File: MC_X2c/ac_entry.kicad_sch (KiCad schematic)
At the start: 16 parts, among them U1 R-78E3.3-1.0

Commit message: Working progress - migration to MAC
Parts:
- renumbered U1 to U2
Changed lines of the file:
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@@
 	(title_block
 		(title "AC Entry")
-		(date "2025-06-1")
+		(date "2025-06-27")
 		(rev "1.0")
 		(company "Nelees")
@@
 		(dnp no)
 		(fields_autoplaced yes)
-		(property "Reference" "U1"
+		(property "Reference" "U2"
 			(at 194.31 36.83 0)
 			(effects
@@
 			(project "MC_X2c"
 				(path "/7c61db7a-af98-4251-97f0-4a36956e03cd/b18795d0-8482-4f6f-8249-1321515800c6"
-					(reference "U1")
-					(unit 1)
-				)
+					(reference "U2")
+					(unit 1)
+				)

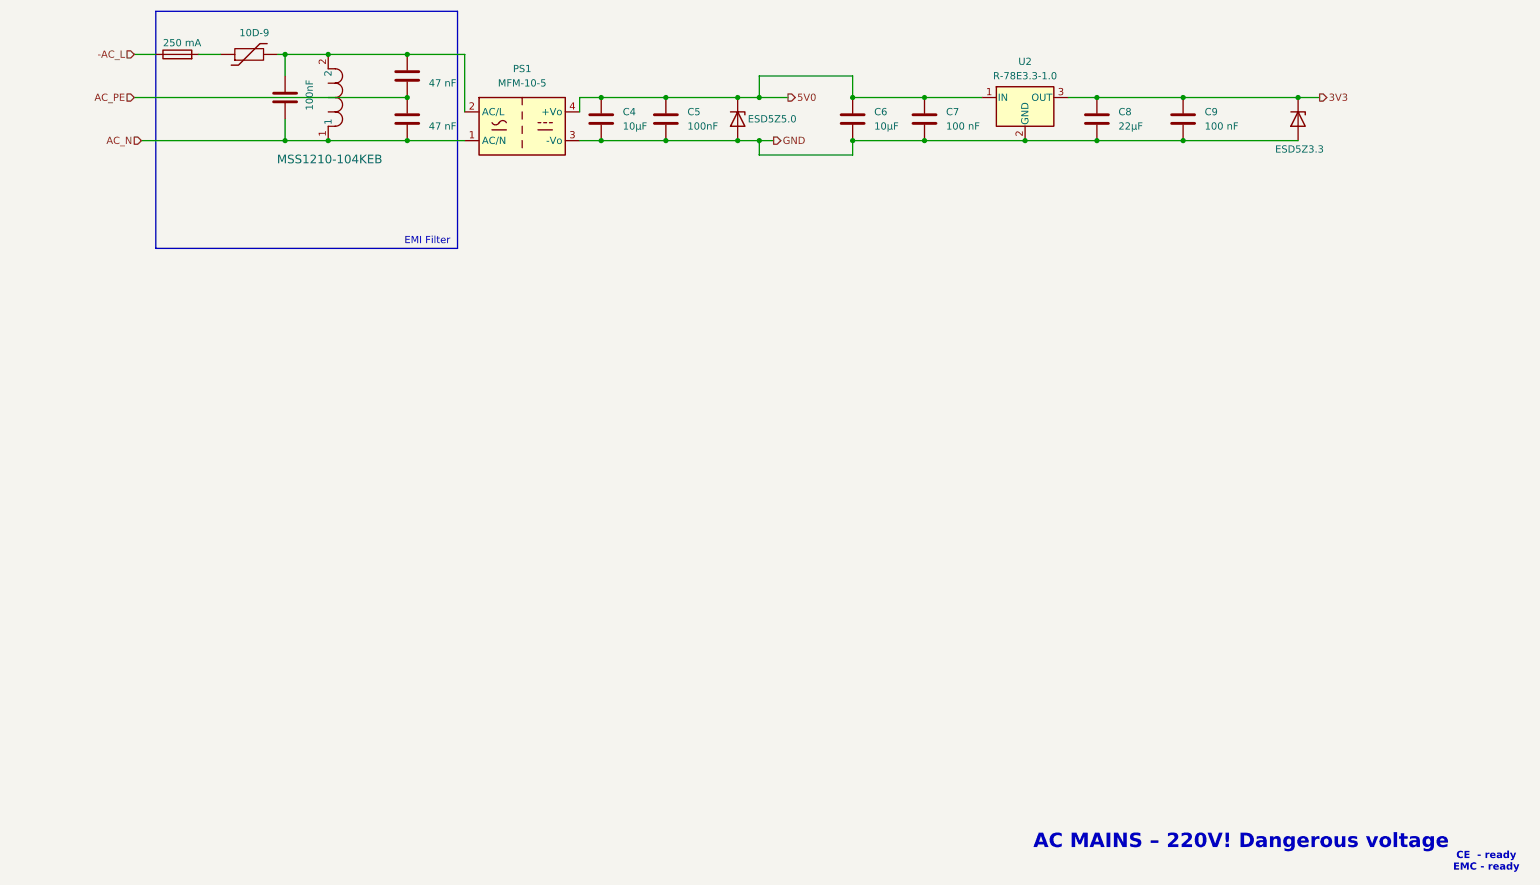
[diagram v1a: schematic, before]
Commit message: Proper namings in AC_ENTRY and CHANNEL + passives on root
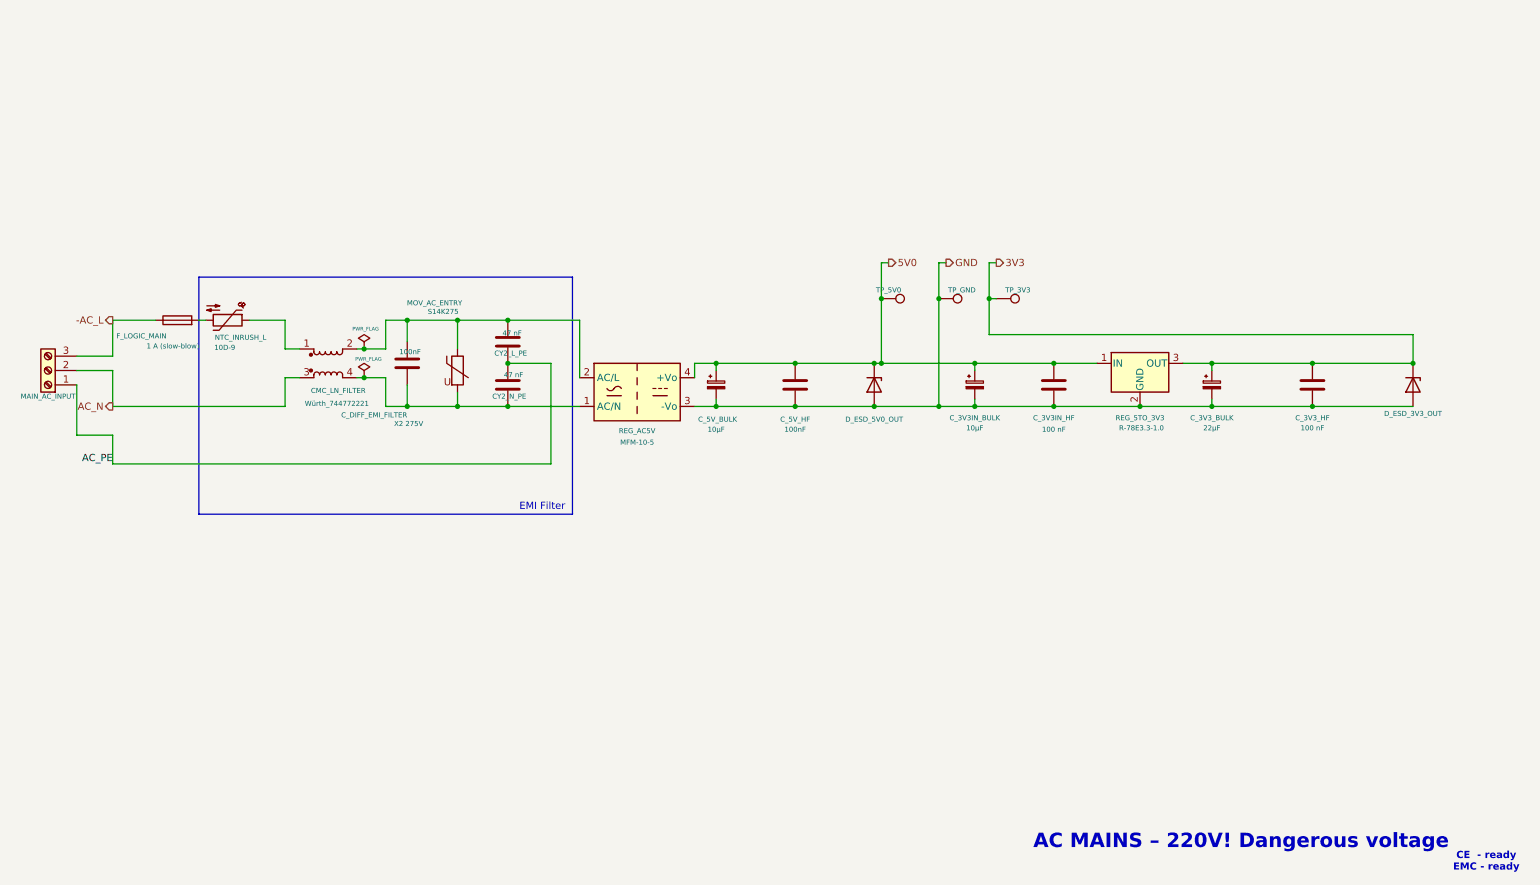
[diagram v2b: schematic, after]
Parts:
- removed C6: 10µF, symbol Device:C
- removed L1: MSS1210-104KEB, IND_MSS1210_COC, symbol nelees:MSS1210-104KEB
- removed TH1: 10D-9, symbol Device:Thermistor
- added CMC_LN_FILTER: Würth_744772221, Inductor_SMD:L_Wuerth_WE-DD-Typ-L-Typ-XL-Typ-XXL, symbol Device:L_Coupled
- added C_3V3IN_BULK: 10µF, symbol Device:C_Polarized_Small
- added MAIN_AC_INPUT: Screw_Terminal_01x03, symbol Connector:Screw_Terminal_01x03
- added MOV_AC_ENTRY: S14K275, symbol Device:Varistor
- added NTC_INRUSH_L: 10D-9, symbol Device:Thermistor_NTC
- added TP2: TP_3V3, TestPoint:TestPoint_Pad_1.0x1.0mm, symbol Connector:TestPoint
- added TP3: TP_GND, TestPoint:TestPoint_Pad_1.0x1.0mm, symbol Connector:TestPoint
- added TP_5V0: TP_5V0, TestPoint:TestPoint_Pad_1.0x1.0mm, symbol Connector:TestPoint
- C_3V3_BULK: renamed from C8; symbol Device:C -> Device:C_Polarized_Small
- C_5V_BULK: renamed from C4; symbol Device:C -> Device:C_Polarized_Small
- D_ESD_5V0_OUT: renamed from D1; value ESD5Z5.0 -> D_ESD_5V0_OUT
- F_LOGIC_MAIN: renamed from F1; value 250 mA -> 1 A (slow-blow)
- renumbered C2 to CY2_L_PE, C3 to CY2_N_PE, C7 to C_3V3IN_HF, C9 to C_3V3_HF, C5 to C_5V_HF, C1 to C_DIFF_EMI_FILTER, D2 to D_ESD_3V3_OUT, U2 to REG_5TO_3V3, PS1 to REG_AC5V
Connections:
- net 3V3: now also TP2.1
- net 5V0: now also C_3V3IN_BULK.1, TP_5V0.1
- net AC_N: now also CMC_LN_FILTER.3, MAIN_AC_INPUT.2 (Pin_2); no longer CY2_N_PE.2, C_DIFF_EMI_FILTER.2, REG_AC5V.1 (AC/N)
- net AC_PE: now also MAIN_AC_INPUT.1 (Pin_1)
- net GND: now also C_3V3IN_BULK.2, TP3.1
- net ­AC_L: now also MAIN_AC_INPUT.3 (Pin_3)
- net at F_LOGIC_MAIN.2: now also NTC_INRUSH_L.2
- net at CY2_L_PE.1, C_DIFF_EMI_FILTER.1, REG_AC5V.2 (AC/L): now also CMC_LN_FILTER.2, MOV_AC_ENTRY.1
- new net: CMC_LN_FILTER.1, NTC_INRUSH_L.1
- new net: CMC_LN_FILTER.4, CY2_N_PE.2, C_DIFF_EMI_FILTER.2, MOV_AC_ENTRY.2, REG_AC5V.1 (AC/N)
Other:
- moved on the sheet: C_3V3IN_HF, C_3V3_HF, C_5V_HF, REG_5TO_3V3, REG_AC5V

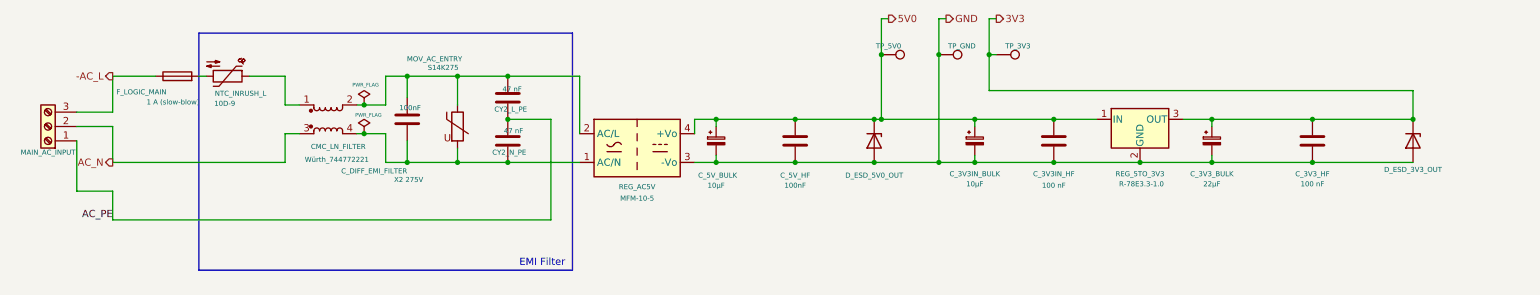
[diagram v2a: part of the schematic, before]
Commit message: Fix channel refference names and add fuse for channel out
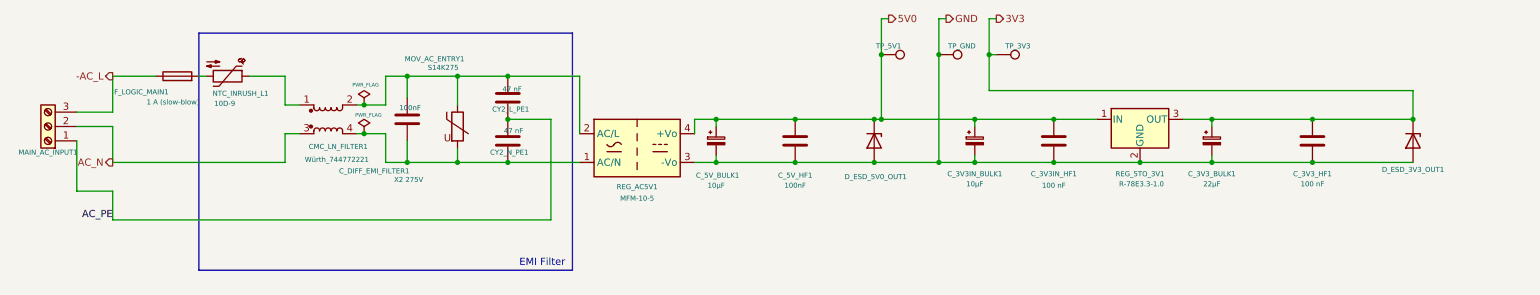
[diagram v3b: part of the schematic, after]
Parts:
- renumbered CMC_LN_FILTER to CMC_LN_FILTER1, CY2_L_PE to CY2_L_PE1, CY2_N_PE to CY2_N_PE1, C_3V3IN_BULK to C_3V3IN_BULK1, C_3V3IN_HF to C_3V3IN_HF1, C_3V3_BULK to C_3V3_BULK1, C_3V3_HF to C_3V3_HF1, C_5V_BULK to C_5V_BULK1, C_5V_HF to C_5V_HF1, C_DIFF_EMI_FILTER to C_DIFF_EMI_FILTER1, D_ESD_3V3_OUT to D_ESD_3V3_OUT1, D_ESD_5V0_OUT to D_ESD_5V0_OUT1, F_LOGIC_MAIN to F_LOGIC_MAIN1, MAIN_AC_INPUT to MAIN_AC_INPUT1, MOV_AC_ENTRY to MOV_AC_ENTRY1, NTC_INRUSH_L to NTC_INRUSH_L1, REG_5TO_3V3 to REG_5TO_3V1, REG_AC5V to REG_AC5V1, TP3 to TP1, TP_5V0 to TP_5V1
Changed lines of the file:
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@@
 		(on_board yes)
 		(dnp no)
-		(property "Reference" "F_LOGIC_MAIN"
+		(property "Reference" "F_LOGIC_MAIN1"
 			(at 38.1 85.344 90)
 			(effects
@@
 			(project "MC_X2c"
 				(path "/7c61db7a-af98-4251-97f0-4a36956e03cd/b18795d0-8482-4f6f-8249-1321515800c6"
-					(reference "F_LOGIC_MAIN")
+					(reference "F_LOGIC_MAIN1")
 					(unit 1)
 				)
@@
 		(on_board yes)
 		(dnp no)
-		(property "Reference" "D_ESD_5V0_OUT"
-			(at 173.99 93.98 0)
-			(effects
-				(font
-					(size 0.889 0.889)
-				)
-				(hide yes)
+		(property "Reference" "D_ESD_5V0_OUT1"
+			(at 167.894 100.33 90)
+			(effects
+				(font
+					(size 0.889 0.889)
+				)
 			)
 		)
 		(property "Value" "D_ESD_5V0_OUT"
-			(at 167.64 100.076 90)
-			(effects
-				(font
-					(size 0.889 0.889)
-					(color 179 61 255 1)
-				)
+			(at 168.148 102.616 90)
+			(effects
+				(font
+					(size 0.889 0.889)
+					(color 179 61 255 1)
+				)
+				(hide yes)
 			)
 		)
@@
 			(project "MC_X2c"
 				(path "/7c61db7a-af98-4251-97f0-4a36956e03cd/b18795d0-8482-4f6f-8249-1321515800c6"
-					(reference "D_ESD_5V0_OUT")
+					(reference "D_ESD_5V0_OUT1")
 					(unit 1)
 				)
@@
 		(on_board yes)
 		(dnp no)
-		(property "Reference" "CMC_LN_FILTER"
+		(property "Reference" "CMC_LN_FILTER1"
 			(at 72.898 94.996 0)
 			(effects
@@
 			(project ""
 				(path "/7c61db7a-af98-4251-97f0-4a36956e03cd/b18795d0-8482-4f6f-8249-1321515800c6"
-					(reference "CMC_LN_FILTER")
+					(reference "CMC_LN_FILTER1")
 					(unit 1)
 				)
@@
 		(on_board yes)
 		(dnp no)
-		(property "Reference" "REG_AC5V"
+		(property "Reference" "REG_AC5V1"
 			(at 125.73 102.108 0)
 			(effects
@@
 			(project "MC_X2c"
 				(path "/7c61db7a-af98-4251-97f0-4a36956e03cd/b18795d0-8482-4f6f-8249-1321515800c6"
-					(reference "REG_AC5V")
+					(reference "REG_AC5V1")
 					(unit 1)
 				)
@@
 		(on_board yes)
 		(dnp no)
-		(property "Reference" "C_3V3IN_HF"
+		(property "Reference" "C_3V3IN_HF1"
 			(at 199.39 99.822 0)
 			(effects
@@
 			(project "MC_X2c"
 				(path "/7c61db7a-af98-4251-97f0-4a36956e03cd/b18795d0-8482-4f6f-8249-1321515800c6"
-					(reference "C_3V3IN_HF")
+					(reference "C_3V3IN_HF1")
 					(unit 1)
 				)
@@
 		(on_board yes)
 		(dnp no)
-		(property "Reference" "CY2_L_PE"
+		(property "Reference" "CY2_L_PE1"
 			(at 103.378 88.392 0)
 			(effects
@@
 			(project "MC_X2c"
 				(path "/7c61db7a-af98-4251-97f0-4a36956e03cd/b18795d0-8482-4f6f-8249-1321515800c6"
-					(reference "CY2_L_PE")
+					(reference "CY2_L_PE1")
 					(unit 1)
 				)
@@
 		(on_board yes)
 		(dnp no)
-		(property "Reference" "NTC_INRUSH_L"
+		(property "Reference" "NTC_INRUSH_L1"
 			(at 55.626 85.598 90)
 			(effects
@@
 			(project ""
 				(path "/7c61db7a-af98-4251-97f0-4a36956e03cd/b18795d0-8482-4f6f-8249-1321515800c6"
-					(reference "NTC_INRUSH_L")
+					(reference "NTC_INRUSH_L1")
 					(unit 1)
 				)
@@
 		(on_board yes)
 		(dnp no)
-		(property "Reference" "REG_5TO_3V3"
+		(property "Reference" "REG_5TO_3V1"
 			(at 214.63 99.822 0)
 			(effects
@@
 			(project "MC_X2c"
 				(path "/7c61db7a-af98-4251-97f0-4a36956e03cd/b18795d0-8482-4f6f-8249-1321515800c6"
-					(reference "REG_5TO_3V3")
+					(reference "REG_5TO_3V1")
 					(unit 1)
 				)
@@
 		(on_board yes)
 		(dnp no)
-		(property "Reference" "TP_5V0"
+		(property "Reference" "TP_5V1"
 			(at 170.18 77.216 90)
 			(effects
@@
 			(project ""
 				(path "/7c61db7a-af98-4251-97f0-4a36956e03cd/b18795d0-8482-4f6f-8249-1321515800c6"
-					(reference "TP_5V0")
+					(reference "TP_5V1")
 					(unit 1)
 				)
@@
 		(on_board yes)
 		(dnp no)
-		(property "Reference" "CY2_N_PE"
+		(property "Reference" "CY2_N_PE1"
 			(at 103.124 96.012 0)
 			(effects
@@
 			(project "MC_X2c"
 				(path "/7c61db7a-af98-4251-97f0-4a36956e03cd/b18795d0-8482-4f6f-8249-1321515800c6"
-					(reference "CY2_N_PE")
+					(reference "CY2_N_PE1")
 					(unit 1)
 				)
@@
 		(on_board yes)
 		(dnp no)
-		(property "Reference" "C_3V3IN_BULK"
+		(property "Reference" "C_3V3IN_BULK1"
 			(at 185.42 99.822 0)
 			(effects
@@
 			(project "MC_X2c"
 				(path "/7c61db7a-af98-4251-97f0-4a36956e03cd/b18795d0-8482-4f6f-8249-1321515800c6"
-					(reference "C_3V3IN_BULK")
+					(reference "C_3V3IN_BULK1")
 					(unit 1)
 				)
@@
 		(on_board yes)
 		(dnp no)
-		(property "Reference" "TP3"
+		(property "Reference" "TP1"
 			(at 183.6421 81.28 0)
 			(effects
@@
 			(project "MC_X2c"
 				(path "/7c61db7a-af98-4251-97f0-4a36956e03cd/b18795d0-8482-4f6f-8249-1321515800c6"
-					(reference "TP3")
+					(reference "TP1")
 					(unit 1)
 				)
@@
 		(on_board yes)
 		(dnp no)
-		(property "Reference" "C_DIFF_EMI_FILTER"
+		(property "Reference" "C_DIFF_EMI_FILTER1"
 			(at 79.248 99.314 0)
 			(effects
@@
 			(project "MC_X2c"
 				(path "/7c61db7a-af98-4251-97f0-4a36956e03cd/b18795d0-8482-4f6f-8249-1321515800c6"
-					(reference "C_DIFF_EMI_FILTER")
+					(reference "C_DIFF_EMI_FILTER1")
 					(unit 1)
 				)
@@
 		(on_board yes)
 		(dnp no)
-		(property "Reference" "MAIN_AC_INPUT"
+		(property "Reference" "MAIN_AC_INPUT1"
 			(at 21.59 96.012 0)
 			(effects
@@
 			(project ""
 				(path "/7c61db7a-af98-4251-97f0-4a36956e03cd/b18795d0-8482-4f6f-8249-1321515800c6"
-					(reference "MAIN_AC_INPUT")
+					(reference "MAIN_AC_INPUT1")
 					(unit 1)
 				)
@@
 		(on_board yes)
 		(dnp no)
-		(property "Reference" "D_ESD_3V3_OUT"
+		(property "Reference" "D_ESD_3V3_OUT1"
 			(at 262.89 99.06 90)
 			(effects
@@
 			(project "MC_X2c"
 				(path "/7c61db7a-af98-4251-97f0-4a36956e03cd/b18795d0-8482-4f6f-8249-1321515800c6"
-					(reference "D_ESD_3V3_OUT")
+					(reference "D_ESD_3V3_OUT1")
 					(unit 1)
 				)
@@
 		(on_board yes)
 		(dnp no)
-		(property "Reference" "C_5V_BULK"
+		(property "Reference" "C_5V_BULK1"
 			(at 139.954 100.076 0)
 			(effects
@@
 			(project "MC_X2c"
 				(path "/7c61db7a-af98-4251-97f0-4a36956e03cd/b18795d0-8482-4f6f-8249-1321515800c6"
-					(reference "C_5V_BULK")
+					(reference "C_5V_BULK1")
 					(unit 1)
 				)
@@
 		(on_board yes)
 		(dnp no)
-		(property "Reference" "C_5V_HF"
+		(property "Reference" "C_5V_HF1"
 			(at 153.67 100.076 0)
 			(effects
@@
 			(project "MC_X2c"
 				(path "/7c61db7a-af98-4251-97f0-4a36956e03cd/b18795d0-8482-4f6f-8249-1321515800c6"
-					(reference "C_5V_HF")
+					(reference "C_5V_HF1")
 					(unit 1)
 				)
@@
 		(on_board yes)
 		(dnp no)
-		(property "Reference" "MOV_AC_ENTRY"
+		(property "Reference" "MOV_AC_ENTRY1"
 			(at 89.916 79.502 0)
 			(effects
@@
 			(project ""
 				(path "/7c61db7a-af98-4251-97f0-4a36956e03cd/b18795d0-8482-4f6f-8249-1321515800c6"
-					(reference "MOV_AC_ENTRY")
+					(reference "MOV_AC_ENTRY1")
 					(unit 1)
 				)
@@
 		(on_board yes)
 		(dnp no)
-		(property "Reference" "C_3V3_HF"
+		(property "Reference" "C_3V3_HF1"
 			(at 245.11 99.822 0)
 			(effects
@@
 			(project "MC_X2c"
 				(path "/7c61db7a-af98-4251-97f0-4a36956e03cd/b18795d0-8482-4f6f-8249-1321515800c6"
-					(reference "C_3V3_HF")
+					(reference "C_3V3_HF1")
 					(unit 1)
 				)
@@
 		(on_board yes)
 		(dnp no)
-		(property "Reference" "C_3V3_BULK"
+		(property "Reference" "C_3V3_BULK1"
 			(at 227.33 99.822 0)
 			(effects
@@
 			(project "MC_X2c"
 				(path "/7c61db7a-af98-4251-97f0-4a36956e03cd/b18795d0-8482-4f6f-8249-1321515800c6"
-					(reference "C_3V3_BULK")
-					(unit 1)
-				)
+					(reference "C_3V3_BULK1")
+					(unit 1)
+				)

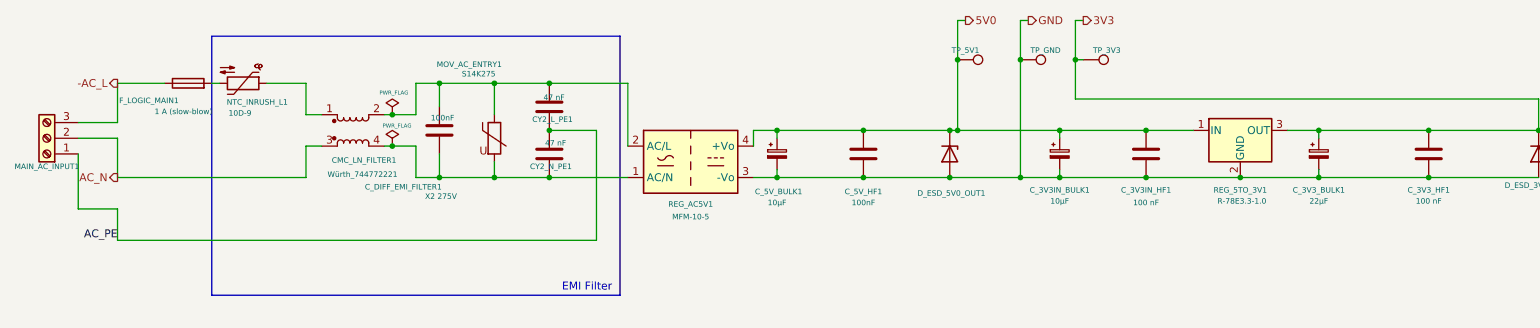
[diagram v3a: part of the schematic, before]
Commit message: Replace MCU with ESP32-S3 and added SPI and RF433 ports
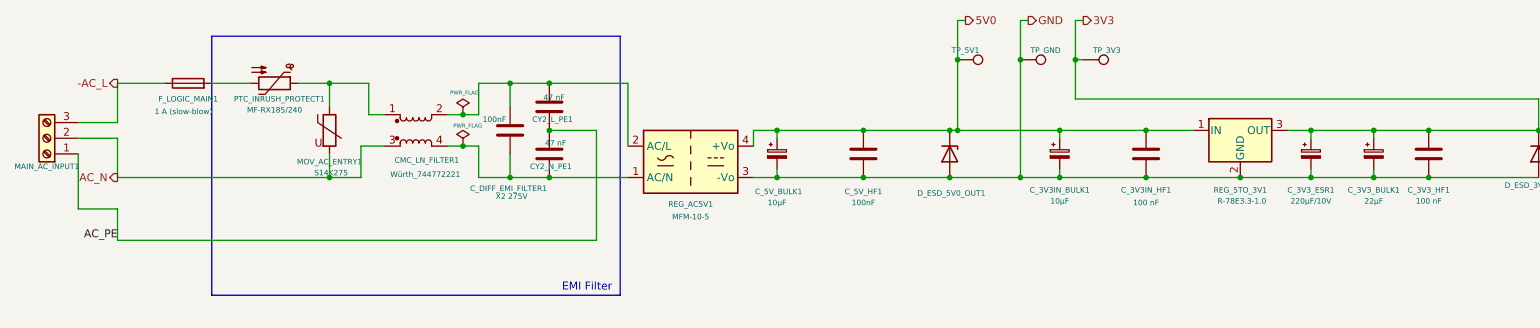
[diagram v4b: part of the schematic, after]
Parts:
- removed NTC_INRUSH_L1: 10D-9, symbol Device:Thermistor_NTC
- added C_3V3_ESR1: 220µF/10V, symbol Device:C_Polarized_Small
- added PTC_INRUSH_PROTECT1: MF-RX185/240, symbol Device:Thermistor_PTC
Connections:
- net 3V3: now also C_3V3_ESR1.1
- net AC_N: now also MOV_AC_ENTRY1.2
- net GND: now also C_3V3_ESR1.2
- net at F_LOGIC_MAIN1.2: now also PTC_INRUSH_PROTECT1.2
- net at CMC_LN_FILTER1.1: now also MOV_AC_ENTRY1.1, PTC_INRUSH_PROTECT1.1
- net at CMC_LN_FILTER1.2, CY2_L_PE1.1, C_DIFF_EMI_FILTER1.1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: no longer MOV_AC_ENTRY1.1
- net at CMC_LN_FILTER1.4, CY2_N_PE1.2, C_DIFF_EMI_FILTER1.2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: no longer MOV_AC_ENTRY1.2
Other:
- moved on the sheet: CMC_LN_FILTER1, C_3V3_BULK1, C_DIFF_EMI_FILTER1, MOV_AC_ENTRY1
